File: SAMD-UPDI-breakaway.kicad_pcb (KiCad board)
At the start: 2 copper layers, 79.1 x 17 mm, 13 parts, among them J1 JTAG, J2 FAB-USB-PCB, J3 FTDI Out, J4 FTDI In, J5 UPDI Out, U1 ATSAMD11C14A-SS, U2 MCP1700

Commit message: Replace RST on JTAG header with Vref.  Labels
ATMEL Ice programmer doesn't use RST, but requires that the target microcontroller's VCC be provided for it to sense.  Remove RST from JTAG header, provide VCC instead.
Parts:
- J1: value JTAG -> SWD
- U2: footprint fab:SOT-23 -> Package_TO_SOT_SMD:SOT-23
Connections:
- J1 pad 3: /*RST -> +3V3
- U1 pad 6: /*RST -> unconnected-(U1-Pad6)
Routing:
- net +3V3: track 23.0 -> 44.1 mm
- net /*RST: track 11.2 -> 0.00 mm
- net GND: track 83.9 -> 85.0 mm
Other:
- board text added: "GND"
- board text added: "U"

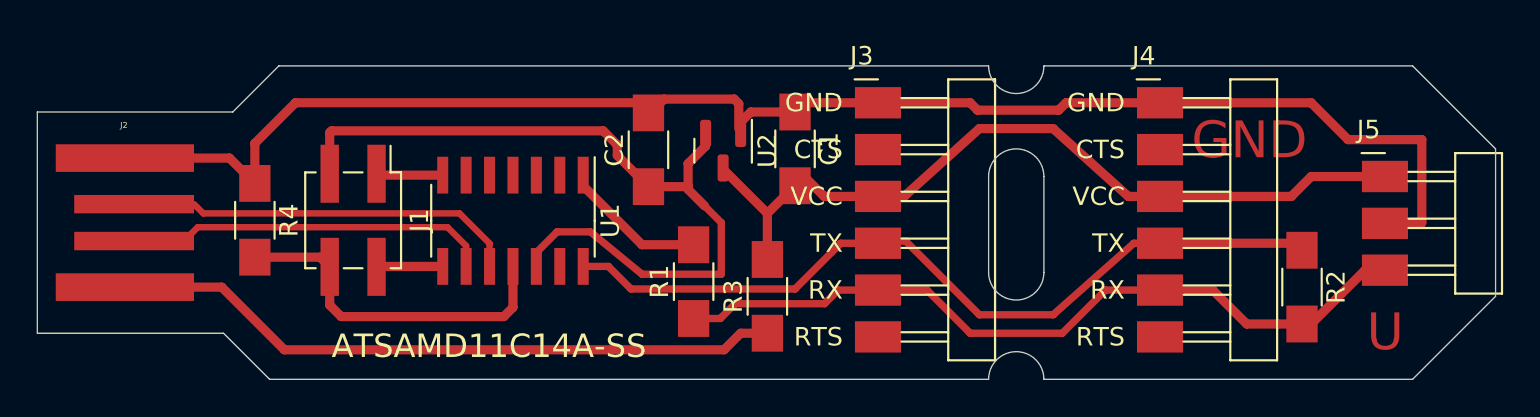
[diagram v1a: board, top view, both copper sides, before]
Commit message: Adjust USB size
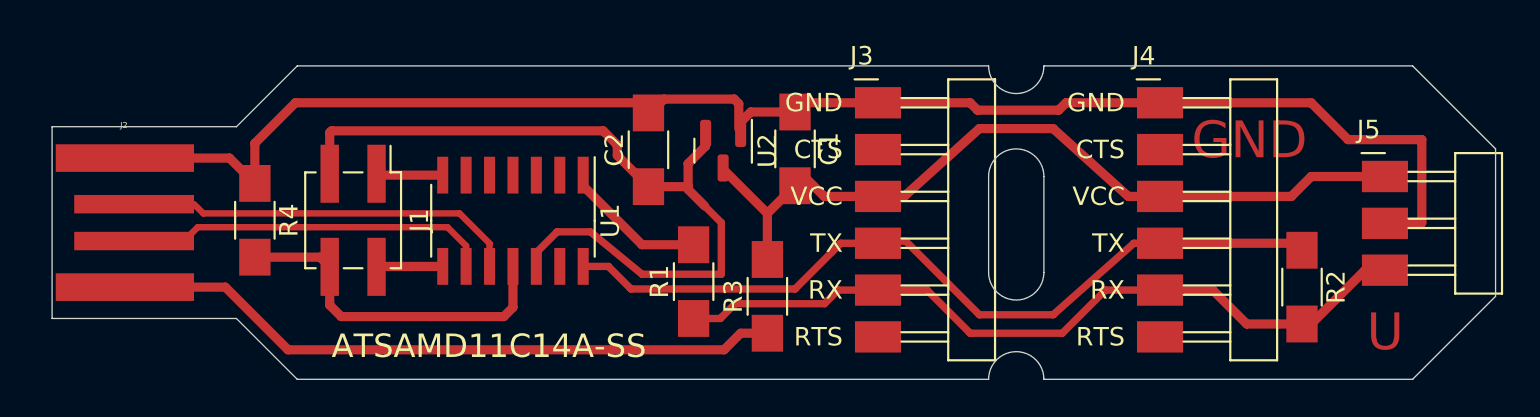
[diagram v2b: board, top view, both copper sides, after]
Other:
- board size 79.1 x 17 mm -> 78.3 x 17 mm
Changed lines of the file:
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@@
   )
   (gr_line (start 54.5 -5.5) (end 54.5 -13.5) (layer "Edge.Cuts") (width 0.05))
-  (gr_line (start -11.5 -18) (end -14 -15.5) (layer "Edge.Cuts") (width 0.05))
-  (gr_line (start -14 -15.5) (end -24.6 -15.5) (layer "Edge.Cuts") (width 0.05))
   (gr_arc (start 30 -18) (mid 28.5 -16.5) (end 27 -18) (layer "Edge.Cuts") (width 0.05))
   (gr_arc (start 27 -1) (mid 28.5 -2.5) (end 30 -1) (layer "Edge.Cuts") (width 0.05))
+  (gr_line (start -10.5 -18) (end -13.8 -14.7) (layer "Edge.Cuts") (width 0.05))
   (gr_line (start 54.5 -13.5) (end 50 -18) (layer "Edge.Cuts") (width 0.05))
   (gr_line (start 27 -6.8) (end 27 -12) (layer "Edge.Cuts") (width 0.05))
+  (gr_line (start -23.8 -14.7) (end -23.8 -4.3) (layer "Edge.Cuts") (width 0.05))
   (gr_line (start 30 -1) (end 50 -1) (layer "Edge.Cuts") (width 0.05))
   (gr_line (start 30 -12) (end 30 -6.8) (layer "Edge.Cuts") (width 0.05))
-  (gr_line (start -24.6 -15.5) (end -24.6 -3.5) (layer "Edge.Cuts") (width 0.05))
-  (gr_line (start 27 -18) (end -11.5 -18) (layer "Edge.Cuts") (width 0.05))
+  (gr_line (start 27 -18) (end -10.5 -18) (layer "Edge.Cuts") (width 0.05))
   (gr_arc (start 30 -6.8) (mid 28.5 -5.3) (end 27 -6.8) (layer "Edge.Cuts") (width 0.05))
+  (gr_line (start -23.8 -4.3) (end -13.8 -4.3) (layer "Edge.Cuts") (width 0.05))
   (gr_line (start 50 -1) (end 54.5 -5.5) (layer "Edge.Cuts") (width 0.05))
   (gr_line (start 30 -18) (end 50 -18) (layer "Edge.Cuts") (width 0.05))
-  (gr_line (start -14.5 -3.5) (end -12 -1) (layer "Edge.Cuts") (width 0.05))
-  (gr_line (start -24.6 -3.5) (end -14.5 -3.5) (layer "Edge.Cuts") (width 0.05))
+  (gr_line (start -13.8 -4.3) (end -10.5 -1) (layer "Edge.Cuts") (width 0.05))
+  (gr_line (start -13.8 -14.7) (end -23.8 -14.7) (layer "Edge.Cuts") (width 0.05))
   (gr_arc (start 27 -12) (mid 28.5 -13.5) (end 30 -12) (layer "Edge.Cuts") (width 0.05))
-  (gr_line (start 27 -1) (end -12 -1) (layer "Edge.Cuts") (width 0.05))
+  (gr_line (start 27 -1) (end -10.5 -1) (layer "Edge.Cuts") (width 0.05))
   (gr_rect (start -26 -19.4) (end 56.2 0.2) (layer "Margin") (width 0.1) (fill none))
   (gr_text "GND" (at 41.148 -13.97) (layer "F.Cu")
@@
   (segment (start -2.61 -12.075) (end -6.125 -12.075) (width 0.5) (layer "F.Cu") (net 11))
   (segment (start -6.125 -12.075) (end -6.2 -12.15) (width 0.5) (layer "F.Cu") (net 11))
-  (segment (start -14.6 -6) (end -11.2 -2.6) (width 0.5) (layer "F.Cu") (net 12))
-  (segment (start -19.85 -6) (end -14.6 -6) (width 0.5) (layer "F.Cu") (net 12))
+  (segment (start -11 -2.6) (end 12.65 -2.6) (width 0.5) (layer "F.Cu") (net 12))
+  (segment (start -14.4 -6) (end -11 -2.6) (width 0.5) (layer "F.Cu") (net 12))
+  (segment (start 13.55 -3.5) (end 15 -3.5) (width 0.5) (layer "F.Cu") (net 12))
+  (segment (start -19.85 -6) (end -14.4 -6) (width 0.5) (layer "F.Cu") (net 12))
   (segment (start 12.65 -2.6) (end 13.55 -3.5) (width 0.5) (layer "F.Cu") (net 12))
-  (segment (start -11.2 -2.6) (end 12.65 -2.6) (width 0.5) (layer "F.Cu") (net 12))
-  (segment (start 13.55 -3.5) (end 15 -3.5) (width 0.5) (layer "F.Cu") (net 12))
   (segment (start 0.7 -4.4) (end -8.115 -4.4) (width 0.5) (layer "F.Cu") (net 13))
   (segment (start 1.2 -4.9) (end 0.7 -4.4) (width 0.5) (layer "F.Cu") (net 13))
